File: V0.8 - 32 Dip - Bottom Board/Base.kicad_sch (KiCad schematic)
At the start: 17 parts, among them J1 Conn_01x20_Socket, J2 Conn_01x20_Socket, J4 Conn_01x16_Pin, J5 Conn_01x16_Pin, U1 74CBTD3861, U2 74LVC1G332, U3 MC74VHC1GT125, U5 74CBTD3861, U6 74CBTD3861, U7 74VHCT245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

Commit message: added mounting holes to 0.1 headers
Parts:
- J1, J2: footprint Connector_PinSocket_1.00mm:PinSocket_2x10_P1.00mm_Vertical_SMD -> JJGTechnologies_Footprint_Library:PinSocket_2x10_P1.00mm_Vertical_SMD
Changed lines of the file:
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@@
 			)
 		)
-		(property "Footprint" "Connector_PinSocket_1.00mm:PinSocket_2x10_P1.00mm_Vertical_SMD"
+		(property "Footprint" "JJGTechnologies_Footprint_Library:PinSocket_2x10_P1.00mm_Vertical_SMD"
 			(at 54.61 44.45 0)
 			(effects
@@
 			)
 		)
-		(property "Datasheet" "~"
+		(property "Datasheet" "FHBD-SS020G1NBWL-FA4"
 			(at 54.61 44.45 0)
 			(effects
@@
 			)
 		)
-		(property "Footprint" "Connector_PinSocket_1.00mm:PinSocket_2x10_P1.00mm_Vertical_SMD"
+		(property "Footprint" "JJGTechnologies_Footprint_Library:PinSocket_2x10_P1.00mm_Vertical_SMD"
 			(at 43.18 44.45 0)
 			(effects
@@
 			)
 		)
-		(property "Datasheet" "~"
+		(property "Datasheet" "FHBD-SS020G1NBWL-FA4"
 			(at 43.18 44.45 0)
 			(effects

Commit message: Logic OR fix
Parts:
- removed U2: 74LVC1G332, Package_TO_SOT_SMD:SOT-363_SC-70-6, symbol JJG_Symbol_Library:74LVC1G332
- added R1: 20k, Resistor_SMD:R_0402_1005Metric, symbol Device:R
- added U2: 74AHC1G32, Package_TO_SOT_SMD:SOT-353_SC-70-5, symbol 74xGxx:74AHC1G32
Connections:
- net 5v: now also R1.2, U2.3 (GND)
- net GND: now also U2.5 (VCC); no longer U3.1
- net ~{3v3-BusConnect}: now also U3.1; no longer U3.2
- net ~{CE}: now also U2.1
- net ~{OE}: now also U2.2
- net at U3.4: now also U7.19 (CE), R1.1
- new net: U2.4, U3.2
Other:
- moved on the sheet: C10, U3

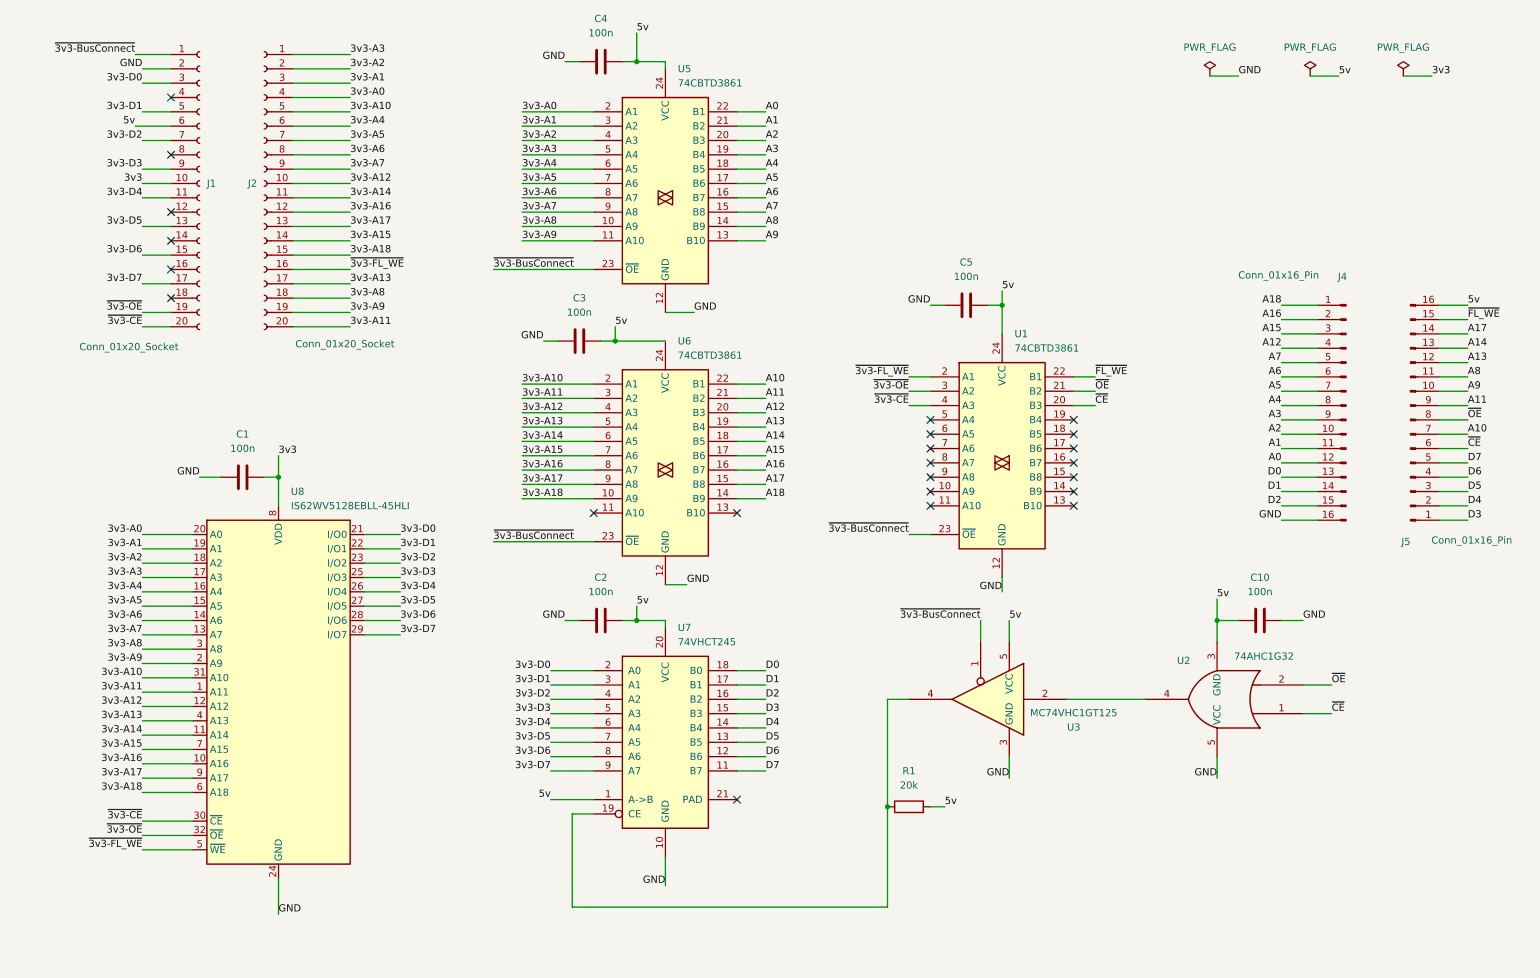
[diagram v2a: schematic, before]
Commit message: Removed Buffer updated Or logic.
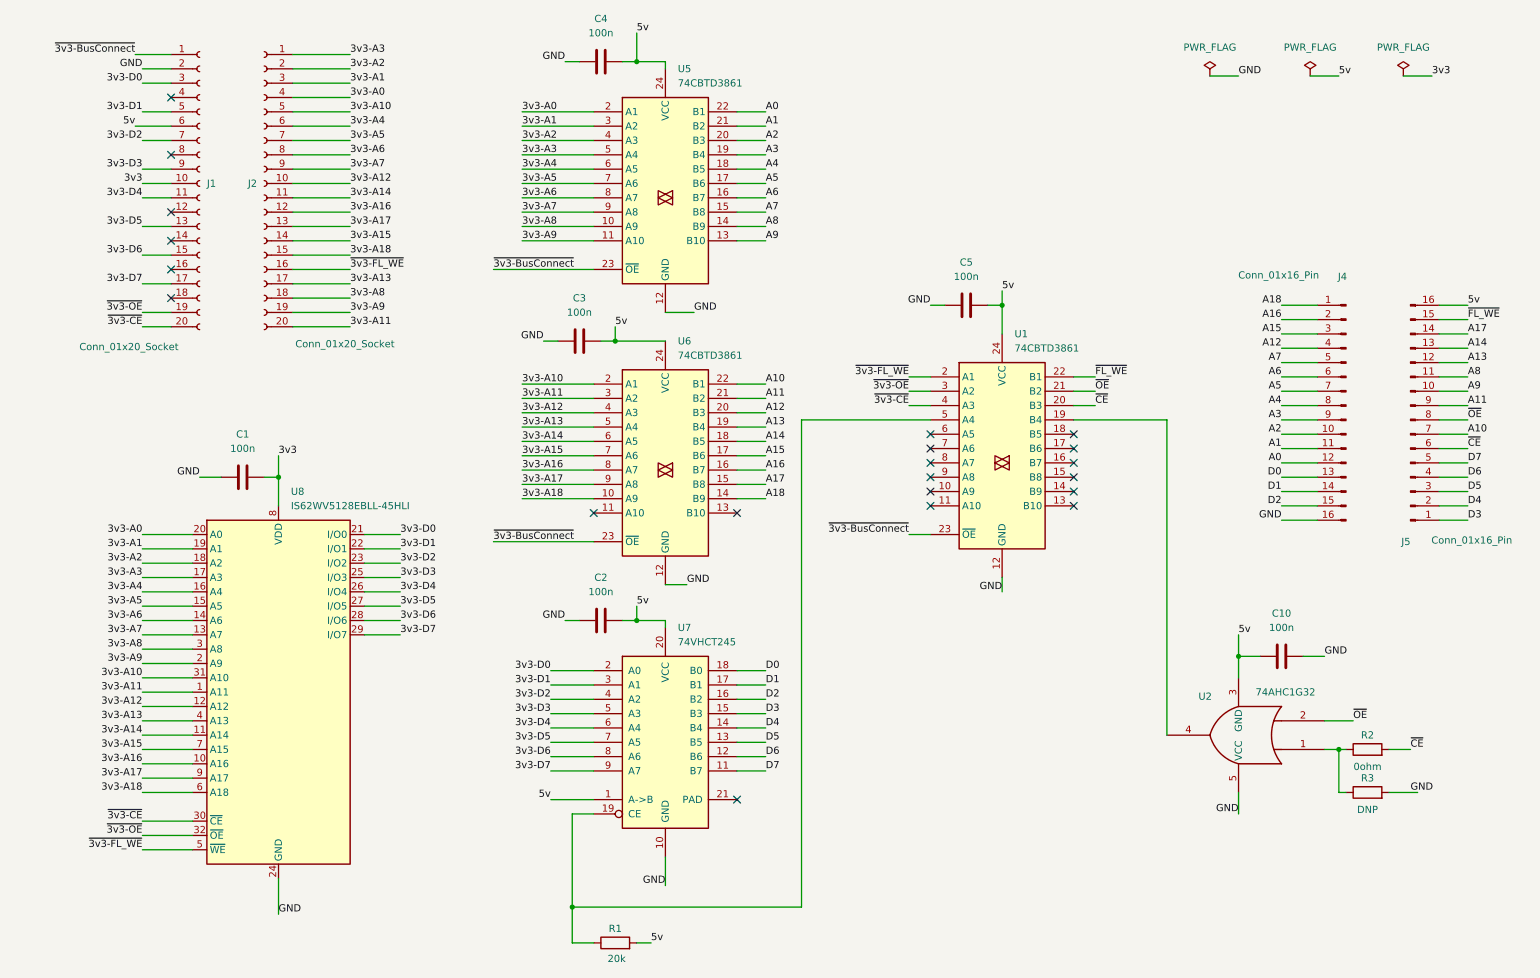
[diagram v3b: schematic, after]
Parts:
- removed U3: MC74VHC1GT125, Package_TO_SOT_SMD:SOT-353_SC-70-5, symbol JJG_Symbol_Library:MC74VHC1GT125
- added R2: 0ohm, Resistor_SMD:R_0402_1005Metric, symbol Device:R
- added R3: DNP, Resistor_SMD:R_0402_1005Metric, symbol Device:R
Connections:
- net GND: now also R3.2
- net ~{CE}: now also R2.2; no longer U2.1
- net at U2.4: now also U1.19 (B4)
- net at R1.1, U7.19 (CE): now also U1.5 (A4)
- new net: R2.1, R3.1, U2.1
- no-connect marks 23 -> 21
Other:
- moved on the sheet: C10, R1, U2
